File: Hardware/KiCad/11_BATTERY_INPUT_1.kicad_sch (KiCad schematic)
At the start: 0 parts

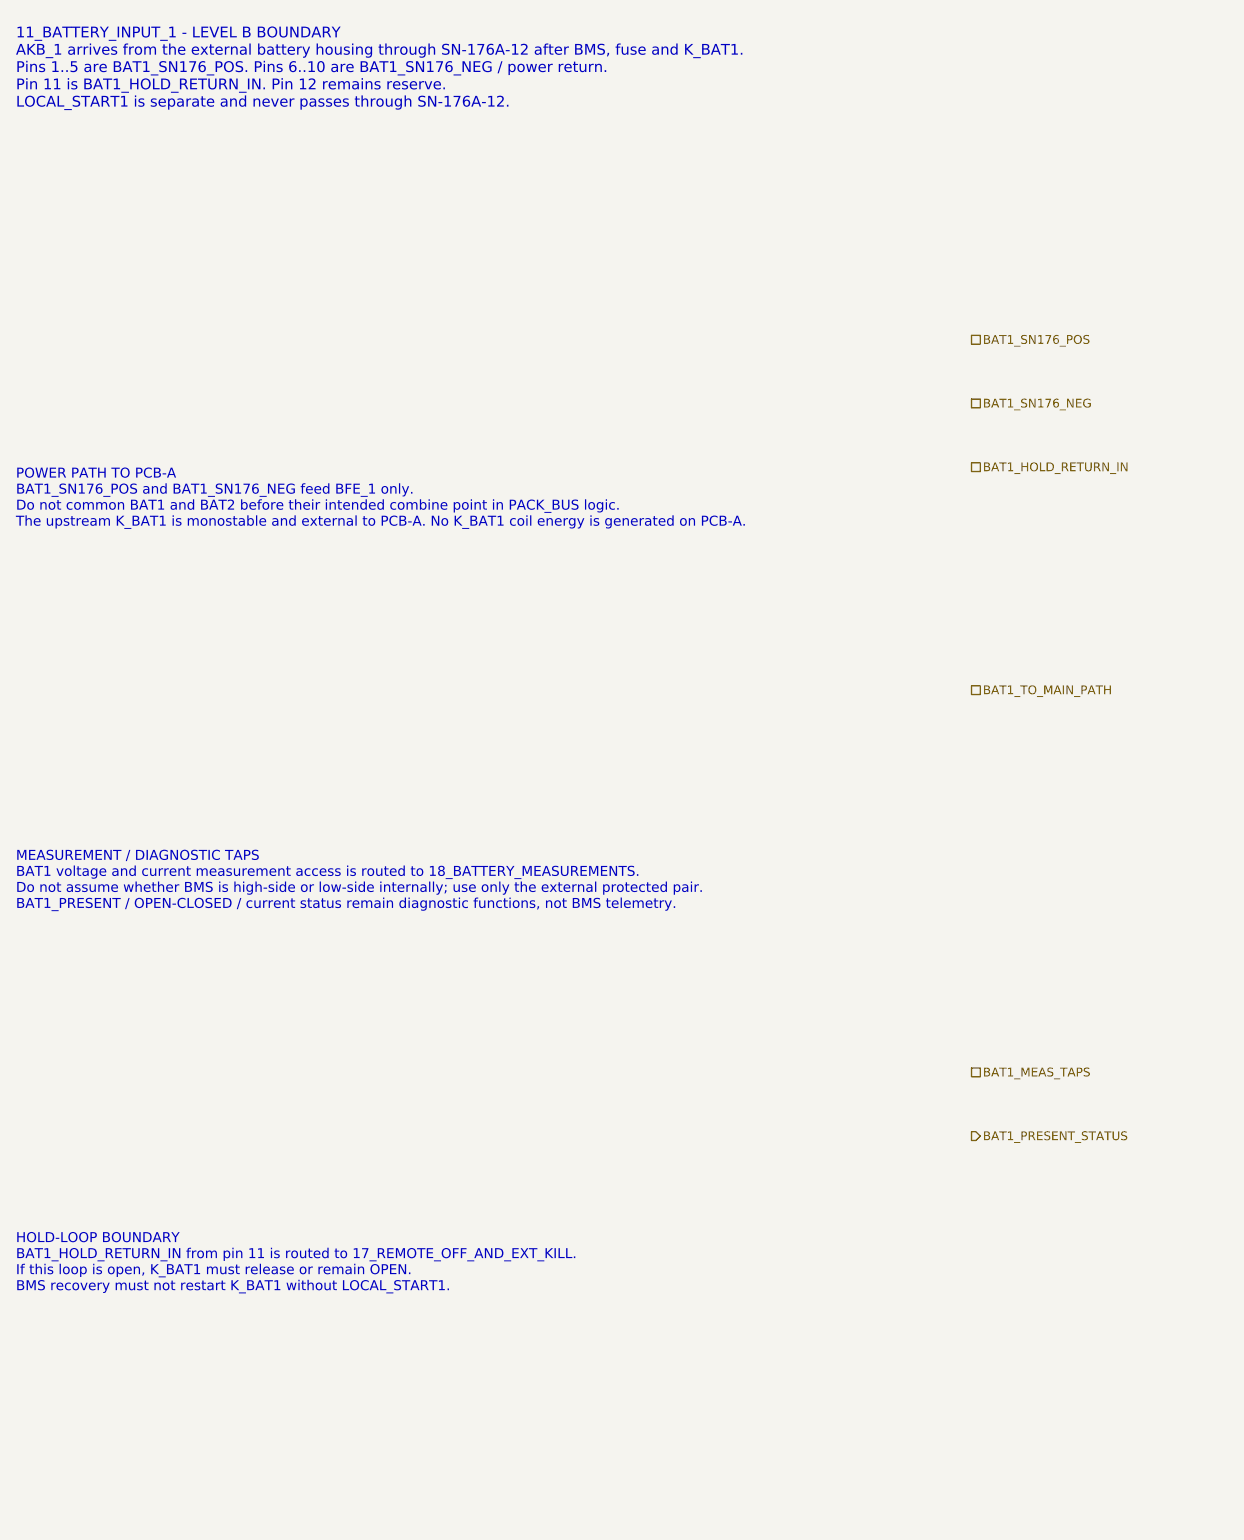
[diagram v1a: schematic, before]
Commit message: hardware: add BAT1 input symbol skeleton zones
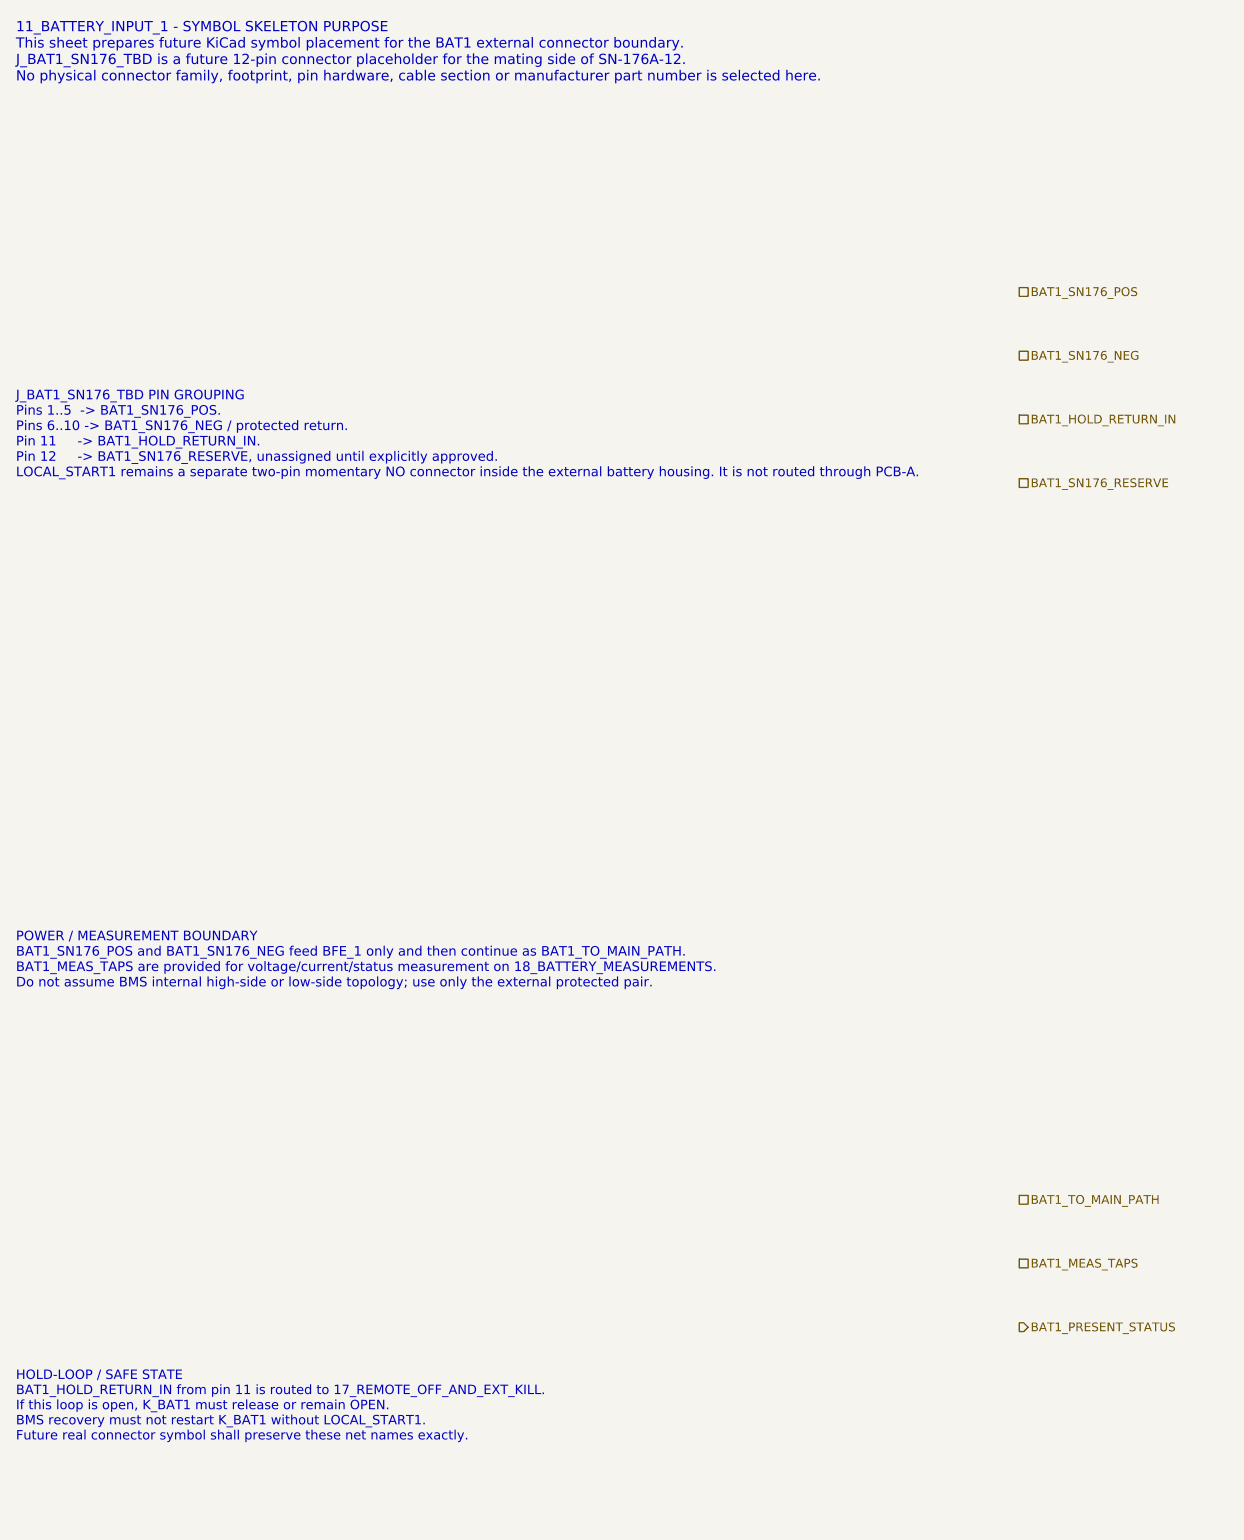
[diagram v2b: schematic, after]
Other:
- note added: "11_BATTERY_INPUT_1 - SYMBOL SKELETON PURPOSE This sheet prepares future KiCad symbol placement for the BAT1 external connector boundary. J_BAT1_SN176_TBD is a future 12-pin connector placeholder for the mating side of SN-176A-12. No physical connector family, footprint, pin hardware, cable section or manufacturer part number is selected here."
- note added: "HOLD-LOOP / SAFE STATE BAT1_HOLD_RETURN_IN from pin 11 is routed to 17_REMOTE_OFF_AND_EXT_KILL. If this loop is open, K_BAT1 must release or remain OPEN. BMS recovery must not restart K_BAT1 without LOCAL_START1. Future real connector symbol shall preserve these net names exactly."
- note added: "J_BAT1_SN176_TBD PIN GROUPING Pins 1..5 -> BAT1_SN176_POS. Pins 6..10 -> BAT1_SN176_NEG / protected return. Pin 11 -> BAT1_HOLD_RETURN_IN. Pin 12 -> BAT1_SN176_RESERVE, unassigned until explicitly approved. LOCAL_START1 remains a separate two-pin momentary NO connector inside the external battery housing. It is not routed through PCB-A."
- note added: "POWER / MEASUREMENT BOUNDARY BAT1_SN176_POS and BAT1_SN176_NEG feed BFE_1 only and then continue as BAT1_TO_MAIN_PATH. BAT1_MEAS_TAPS are provided for voltage/current/status measurement on 18_BATTERY_MEASUREMENTS. Do not assume BMS internal high-side or low-side topology; use only the external protected pair."
- note removed: "11_BATTERY_INPUT_1 - LEVEL B BOUNDARY AKB_1 arrives from the external battery housing through SN-176A-12 after BMS, fuse and K_BAT1. Pins 1..5 are BAT1_SN176_POS. Pins 6..10 are BAT1_SN176_NEG / power return. Pin 11 is BAT1_HOLD_RETURN_IN. Pin 12 remains reserve. LOCAL_START1 is separate and never passes through SN-176A-12."
- note removed: "HOLD-LOOP BOUNDARY BAT1_HOLD_RETURN_IN from pin 11 is routed to 17_REMOTE_OFF_AND_EXT_KILL. If this loop is open, K_BAT1 must release or remain OPEN. BMS recovery must not restart K_BAT1 without LOCAL_START1."
- note removed: "MEASUREMENT / DIAGNOSTIC TAPS BAT1 voltage and current measurement access is routed to 18_BATTERY_MEASUREMENTS. Do not assume whether BMS is high-side or low-side internally; use only the external protected pair. BAT1_PRESENT / OPEN-CLOSED / current status remain diagnostic functions, not BMS telemetry."
- note removed: "POWER PATH TO PCB-A BAT1_SN176_POS and BAT1_SN176_NEG feed BFE_1 only. Do not common BAT1 and BAT2 before their intended combine point in PACK_BUS logic. The upstream K_BAT1 is monostable and external to PCB-A. No K_BAT1 coil energy is generated on PCB-A."
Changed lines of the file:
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@@
 		(title "11_BATTERY_INPUT_1 - BFE input from AKB_1")
 		(date "2026-07-15")
-		(rev "B1")
+		(rev "C0")
 		(company "Gonoboben/plataVM")
-		(comment 1 "Architecture Level B: BAT1 connector boundary and net naming")
-		(comment 2 "No connector family, fuse, current sensor or contactor model selected here")
+		(comment 1 "Symbol skeleton: BAT1 SN-176A-12 boundary and future connector placement zones")
+		(comment 2 "Text-only placeholders; no connector family, footprint, fuse, sensor or contactor selected")
 	)
-	(text "11_BATTERY_INPUT_1 - LEVEL B BOUNDARY\nAKB_1 arrives from the external battery housing through SN-176A-12 after BMS, fuse and K_BAT1.\nPins 1..5 are BAT1_SN176_POS. Pins 6..10 are BAT1_SN176_NEG / power return.\nPin 11 is BAT1_HOLD_RETURN_IN. Pin 12 remains reserve.\nLOCAL_START1 is separate and never passes through SN-176A-12."
+	(text "11_BATTERY_INPUT_1 - SYMBOL SKELETON PURPOSE\nThis sheet prepares future KiCad symbol placement for the BAT1 external connector boundary.\nJ_BAT1_SN176_TBD is a future 12-pin connector placeholder for the mating side of SN-176A-12.\nNo physical connector family, footprint, pin hardware, cable section or manufacturer part number is selected here."
 		(exclude_from_sim no)
-		(at 12 16 0)
-		(effects (font (size 1.35 1.35)) (justify left))
-		(uuid "bfe-dh-00000011-0000-4000-8000-000000000101")
+		(at 12 14 0)
+		(effects (font (size 1.28 1.28)) (justify left))
+		(uuid "bfe-symbol-00000011-0000-4000-8000-000000000101")
 	)
-	(text "POWER PATH TO PCB-A\nBAT1_SN176_POS and BAT1_SN176_NEG feed BFE_1 only.\nDo not common BAT1 and BAT2 before their intended combine point in PACK_BUS logic.\nThe upstream K_BAT1 is monostable and external to PCB-A. No K_BAT1 coil energy is generated on PCB-A."
+	(text "J_BAT1_SN176_TBD PIN GROUPING\nPins 1..5  -> BAT1_SN176_POS.\nPins 6..10 -> BAT1_SN176_NEG / protected return.\nPin 11     -> BAT1_HOLD_RETURN_IN.\nPin 12     -> BAT1_SN176_RESERVE, unassigned until explicitly approved.\nLOCAL_START1 remains a separate two-pin momentary NO connector inside the external battery housing. It is not routed through PCB-A."
 		(exclude_from_sim no)
-		(at 12 70 0)
-		(effects (font (size 1.25 1.25)) (justify left))
-		(uuid "bfe-dh-00000011-0000-4000-8000-000000000102")
+		(at 12 62 0)
+		(effects (font (size 1.20 1.20)) (justify left))
+		(uuid "bfe-symbol-00000011-0000-4000-8000-000000000102")
 	)
-	(text "MEASUREMENT / DIAGNOSTIC TAPS\nBAT1 voltage and current measurement access is routed to 18_BATTERY_MEASUREMENTS.\nDo not assume whether BMS is high-side or low-side internally; use only the external protected pair.\nBAT1_PRESENT / OPEN-CLOSED / current status remain diagnostic functions, not BMS telemetry."
+	(text "POWER / MEASUREMENT BOUNDARY\nBAT1_SN176_POS and BAT1_SN176_NEG feed BFE_1 only and then continue as BAT1_TO_MAIN_PATH.\nBAT1_MEAS_TAPS are provided for voltage/current/status measurement on 18_BATTERY_MEASUREMENTS.\nDo not assume BMS internal high-side or low-side topology; use only the external protected pair."
 		(exclude_from_sim no)
-		(at 12 118 0)
-		(effects (font (size 1.25 1.25)) (justify left))
-		(uuid "bfe-dh-00000011-0000-4000-8000-000000000103")
+		(at 12 128 0)
+		(effects (font (size 1.20 1.20)) (justify left))
+		(uuid "bfe-symbol-00000011-0000-4000-8000-000000000103")
 	)
-	(text "HOLD-LOOP BOUNDARY\nBAT1_HOLD_RETURN_IN from pin 11 is routed to 17_REMOTE_OFF_AND_EXT_KILL.\nIf this loop is open, K_BAT1 must release or remain OPEN.\nBMS recovery must not restart K_BAT1 without LOCAL_START1."
+	(text "HOLD-LOOP / SAFE STATE\nBAT1_HOLD_RETURN_IN from pin 11 is routed to 17_REMOTE_OFF_AND_EXT_KILL.\nIf this loop is open, K_BAT1 must release or remain OPEN.\nBMS recovery must not restart K_BAT1 without LOCAL_START1.\nFuture real connector symbol shall preserve these net names exactly."
 		(exclude_from_sim no)
-		(at 12 166 0)
-		(effects (font (size 1.25 1.25)) (justify left))
-		(uuid "bfe-dh-00000011-0000-4000-8000-000000000104")
+		(at 12 184 0)
+		(effects (font (size 1.18 1.18)) (justify left))
+		(uuid "bfe-symbol-00000011-0000-4000-8000-000000000104")
 	)
-	(hierarchical_label "BAT1_SN176_POS" (shape passive) (exclude_from_sim no) (at 132 50 0) (effects (font (size 1.1 1.1)) (justify left)) (uuid "bfe-dh-00000011-0000-4000-8000-000000000201"))
-	(hierarchical_label "BAT1_SN176_NEG" (shape passive) (exclude_from_sim no) (at 132 58 0) (effects (font (size 1.1 1.1)) (justify left)) (uuid "bfe-dh-00000011-0000-4000-8000-000000000202"))
-	(hierarchical_label "BAT1_HOLD_RETURN_IN" (shape passive) (exclude_from_sim no) (at 132 66 0) (effects (font (size 1.1 1.1)) (justify left)) (uuid "bfe-dh-00000011-0000-4000-8000-000000000203"))
-	(hierarchical_label "BAT1_TO_MAIN_PATH" (shape passive) (exclude_from_sim no) (at 132 94 0) (effects (font (size 1.1 1.1)) (justify left)) (uuid "bfe-dh-00000011-0000-4000-8000-000000000204"))
-	(hierarchical_label "BAT1_MEAS_TAPS" (shape passive) (exclude_from_sim no) (at 132 142 0) (effects (font (size 1.1 1.1)) (justify left)) (uuid "bfe-dh-00000011-0000-4000-8000-000000000205"))
-	(hierarchical_label "BAT1_PRESENT_STATUS" (shape output) (exclude_from_sim no) (at 132 150 0) (effects (font (size 1.1 1.1)) (justify left)) (uuid "bfe-dh-00000011-0000-4000-8000-000000000206"))
+	(hierarchical_label "BAT1_SN176_POS" (shape passive) (exclude_from_sim no) (at 138 44 0) (effects (font (size 1.1 1.1)) (justify left)) (uuid "bfe-symbol-00000011-0000-4000-8000-000000000201"))
+	(hierarchical_label "BAT1_SN176_NEG" (shape passive) (exclude_from_sim no) (at 138 52 0) (effects (font (size 1.1 1.1)) (justify left)) (uuid "bfe-symbol-00000011-0000-4000-8000-000000000202"))
+	(hierarchical_label "BAT1_HOLD_RETURN_IN" (shape passive) (exclude_from_sim no) (at 138 60 0) (effects (font (size 1.1 1.1)) (justify left)) (uuid "bfe-symbol-00000011-0000-4000-8000-000000000203"))
+	(hierarchical_label "BAT1_SN176_RESERVE" (shape passive) (exclude_from_sim no) (at 138 68 0) (effects (font (size 1.1 1.1)) (justify left)) (uuid "bfe-symbol-00000011-0000-4000-8000-000000000204"))
+	(hierarchical_label "BAT1_TO_MAIN_PATH" (shape passive) (exclude_from_sim no) (at 138 158 0) (effects (font (size 1.1 1.1)) (justify left)) (uuid "bfe-symbol-00000011-0000-4000-8000-000000000205"))
+	(hierarchical_label "BAT1_MEAS_TAPS" (shape passive) (exclude_from_sim no) (at 138 166 0) (effects (font (size 1.1 1.1)) (justify left)) (uuid "bfe-symbol-00000011-0000-4000-8000-000000000206"))
+	(hierarchical_label "BAT1_PRESENT_STATUS" (shape output) (exclude_from_sim no) (at 138 174 0) (effects (font (size 1.1 1.1)) (justify left)) (uuid "bfe-symbol-00000011-0000-4000-8000-000000000207"))
 )
